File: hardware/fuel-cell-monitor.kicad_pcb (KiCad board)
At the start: 2 copper layers, 63.5 x 85 mm, 25 parts, among them M1 Solution pump, M2 Air pump, P1 Power in, P2 Fuel cell, P3 Load, P4 Sense check, Q1 2N7000, SW1 Write control, U1 Temperature sensor

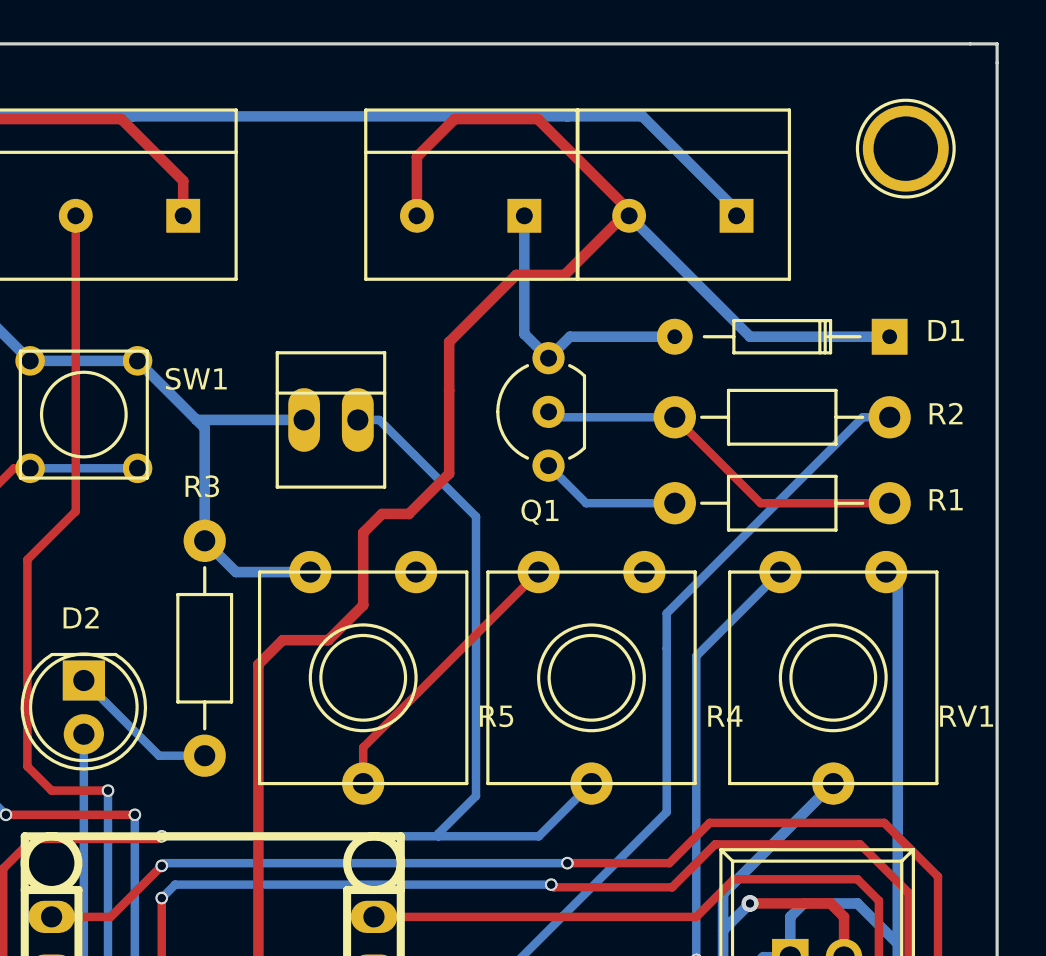
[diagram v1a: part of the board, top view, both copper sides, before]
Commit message: Final fixes before ordering pcbs.
Most notably solution pump driver mosfet had to be changed. The earlier
specified type did not work.
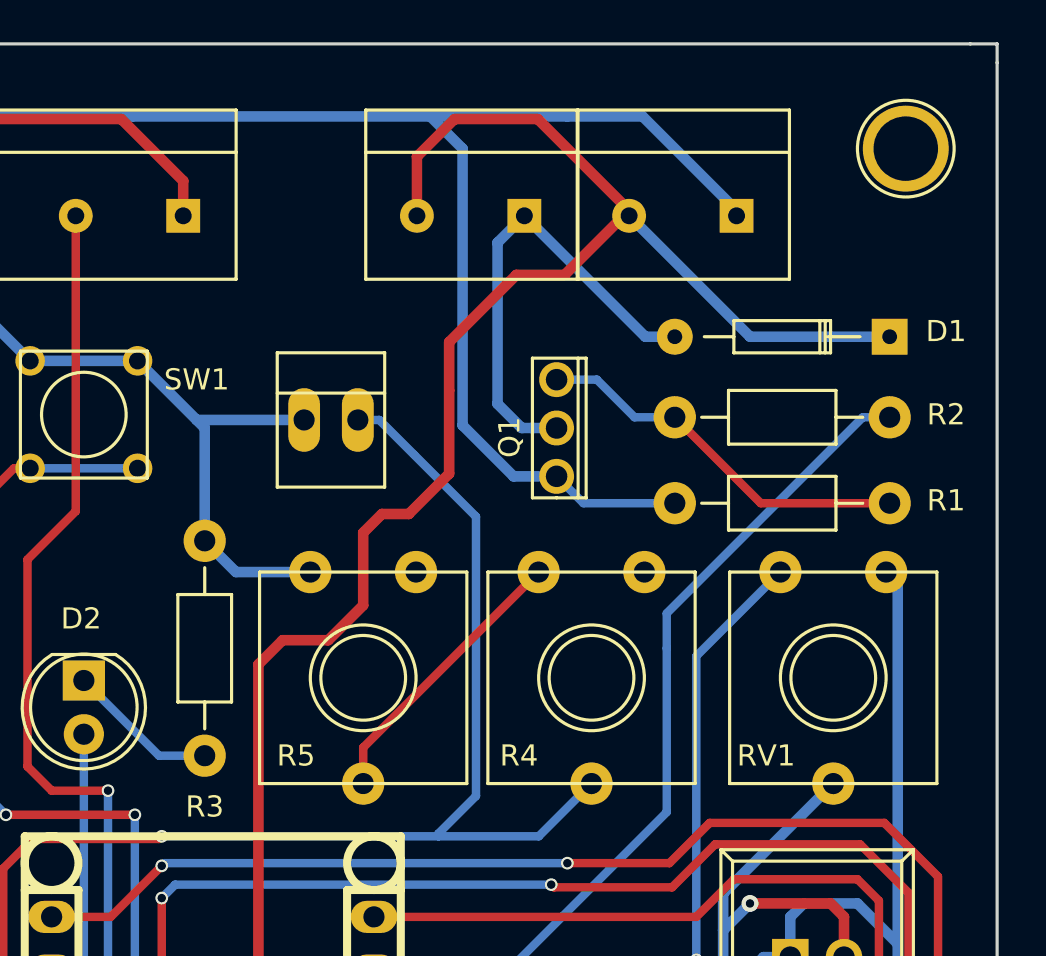
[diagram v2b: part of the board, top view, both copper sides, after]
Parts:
- Q1: value 2N7000 -> IRLLU024N; footprint TO_SOT_Packages_THT:TO-92_Inline_Wide -> TO_SOT_Packages_THT:TO-251AA
- S1: value Opacity sensor -> Opacity_sensor
- S2: value Light sensor -> Light_level_sensor
- SW1: value Write control -> Write_control
- moved Q1 4.08 mm to (157.4, 74.3), turned to 270 degrees
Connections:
- Q1 pad 2: Net-(Q1-Pad2) -> Net-(D1-Pad2)
- Q1 pad 3: Net-(D1-Pad2) -> GND
- R1 pad 1: Net-(Q1-Pad2) -> Net-(Q1-Pad1)
- R1 pad 2: Net-(Q1-Pad1) -> GND
- R2 pad 2: Net-(Q1-Pad2) -> Net-(Q1-Pad1)
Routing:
- net GND: track 290.4 -> 317.2 mm
- net Net-(Q1-Pad2): track 17.9 -> 0.00 mm
- net Net-(Q1-Pad1): track 6.71 -> 18.2 mm
- net Net-(D1-Pad2): track 13.9 -> 22.2 mm
